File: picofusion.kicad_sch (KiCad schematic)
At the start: 48 parts, among them J1 NORTH, J2 EAST, J3 WEST, J4 SOUTH, U1 W25Q16, U2 RP2040, U3 TLV71333PDQN, U7 TJA1051TK-3, Y1 12MHz

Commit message: finish R02B
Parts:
- removed 3V3: TestPoint, TestPoint:TestPoint_Pad_1.0x1.0mm, symbol Connector:TestPoint
- added R24: 0, Resistor_SMD:R_0402_1005Metric, symbol Device:R
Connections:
- net SD_nCD: now also R24.2
- net SPI0_nCS: now also R24.1
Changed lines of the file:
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@@
 (kicad_sch (version 20211123) (generator eeschema)
   (paper "A4")
-  (junction (at 204.47 85.09) (diameter 0) (color 0 0 0 0)
-  )
   (junction (at 66.04 24.13) (diameter 0.9144) (color 0 0 0 0)
   )
@@
   (junction (at 99.06 36.83) (diameter 0.9144) (color 0 0 0 0)
   )
-  (no_connect (at 96.52 128.27))
   (no_connect (at 96.52 110.49))
+  (no_connect (at 96.52 128.27))
   (no_connect (at 96.52 130.81))
+  (no_connect (at 96.52 92.71))
   (no_connect (at 96.52 90.17))
   (no_connect (at 96.52 85.09))
-  (no_connect (at 96.52 92.71))
   (wire (pts (xy 96.52 77.47) (xy 114.3 77.47))
     (stroke (width 0) (type default) (color 0 0 0 0))
@@
     (stroke (width 0) (type default) (color 0 0 0 0))
   )
-  (wire (pts (xy 204.47 85.09) (xy 204.47 82.55))
-    (stroke (width 0) (type default) (color 0 0 0 0))
-  )
   (wire (pts (xy 121.92 34.29) (xy 121.92 36.83))
     (stroke (width 0) (type default) (color 0 0 0 0))
@@
     (stroke (width 0) (type solid) (color 0 0 0 0))
   )
+  (wire (pts (xy 219.71 74.93) (xy 237.49 74.93))
+    (stroke (width 0) (type default) (color 0 0 0 0))
+  )
   (wire (pts (xy 96.52 44.45) (xy 113.03 44.45))
     (stroke (width 0) (type solid) (color 0 0 0 0))
@@
     (stroke (width 0) (type default) (color 0 0 0 0))
   )
-  (wire (pts (xy 262.89 74.93) (xy 247.65 74.93))
+  (wire (pts (xy 245.11 74.93) (xy 262.89 74.93))
     (stroke (width 0) (type default) (color 0 0 0 0))
   )
@@
     (stroke (width 0) (type default) (color 0 0 0 0))
   )
-  (wire (pts (xy 199.39 85.09) (xy 204.47 85.09))
+  (wire (pts (xy 199.39 85.09) (xy 207.01 85.09))
     (stroke (width 0) (type default) (color 0 0 0 0))
   )
@@
     (stroke (width 0) (type default) (color 0 0 0 0))
   )
-  (wire (pts (xy 204.47 85.09) (xy 207.01 85.09))
-    (stroke (width 0) (type default) (color 0 0 0 0))
-  )
   (wire (pts (xy 19.05 24.13) (xy 25.4 24.13))
     (stroke (width 0) (type default) (color 0 0 0 0))
@@
     (effects (font (size 1.27 1.27)) (justify right bottom))
   )
+  (label "SPI0_nCS" (at 219.71 74.93 0)
+    (effects (font (size 1.27 1.27)) (justify left bottom))
+  )
   (label "SPI0_PICO" (at 162.56 33.02 0)
     (effects (font (size 1.27 1.27)) (justify left bottom))
@@
     (pin "1")
   )
+  (symbol (lib_id "Device:R") (at 241.3 74.93 90) (unit 1)
+    (in_bom yes) (on_board yes)
+    (property "Reference" "R24" (id 0) (at 241.3 69.85 90))
+    (property "Value" "0" (id 1) (at 241.3 74.93 90))
+    (property "Footprint" "Resistor_SMD:R_0402_1005Metric" (id 2) (at 241.3 76.708 90)
+      (effects (font (size 1.27 1.27)) hide)
+    )
+    (property "Datasheet" "~" (id 3) (at 241.3 74.93 0)
+      (effects (font (size 1.27 1.27)) hide)
+    )
+    (property "DNP" "[DNP]" (id 4) (at 241.3 72.39 90))
+    (pin "1")
+    (pin "2")
+  )
   (symbol (lib_id "Device:C") (at 199.39 91.44 0) (unit 1)
     (in_bom yes) (on_board yes) (fields_autoplaced)
@@
     (pin "1")
   )
-  (symbol (lib_id "Connector:TestPoint") (at 204.47 82.55 0) (unit 1)
-    (in_bom yes) (on_board yes)
-    (property "Reference" "3V3" (id 0) (at 203.2 77.47 0)
-      (effects (font (size 1.27 1.27)) (justify left))
-    )
-    (property "Value" "TestPoint" (id 1) (at 207.01 80.5179 0)
-      (effects (font (size 1.27 1.27)) (justify left) hide)
-    )
-    (property "Footprint" "TestPoint:TestPoint_Pad_1.0x1.0mm" (id 2) (at 209.55 82.55 0)
-      (effects (font (size 1.27 1.27)) hide)
-    )
-    (property "Datasheet" "~" (id 3) (at 209.55 82.55 0)
-      (effects (font (size 1.27 1.27)) hide)
-    )
-    (pin "1")
-  )
   (symbol (lib_id "Device:C") (at 91.44 30.48 0) (unit 1)
     (in_bom yes) (on_board yes)
@@
       (reference "#PWR0111") (unit 1) (value "GND") (footprint "")
     )
-    (path "/5f13a28e-82a1-4e85-b4bc-5dfc256ed5f9"
-      (reference "3V3") (unit 1) (value "TestPoint") (footprint "TestPoint:TestPoint_Pad_1.0x1.0mm")
-    )
     (path "/d7b2b70b-51e8-4c92-820a-d9481fe18140"
       (reference "C1") (unit 1) (value "0.1uF") (footprint "Capacitor_SMD:C_0402_1005Metric")
@@
       (reference "R23") (unit 1) (value "10K") (footprint "Resistor_SMD:R_0402_1005Metric")
     )
+    (path "/1bc91197-611a-43de-a0c8-4847d4e8d56c"
+      (reference "R24") (unit 1) (value "0") (footprint "Resistor_SMD:R_0402_1005Metric")
+    )
     (path "/2b6f5c8a-05cf-4448-8322-d77121105d11"

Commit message: R02B: finish new discussion modifications
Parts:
- removed J1: NORTH, picofusion_stamp:Castellated_1x8_P2.54mm_Vertical, symbol Connector_Generic:Conn_01x08
- removed R22, R24: 0, Resistor_SMD:R_0402_1005Metric, symbol Device:R
- added J1: NORTH, Connector_PinHeader_2.00mm:PinHeader_1x10_P2.00mm_Vertical, symbol Connector_Generic:Conn_01x10
- C1, C10, C11, C13, C15, C2, C24, C26, C27, C28, C4, C6, C7, C9: footprint Capacitor_SMD:C_0402_1005Metric -> Capacitor_SMD:C_0201_0603Metric; Mfr. # (none) -> CC0201KRX5R5BB104
- C14, C16: footprint Capacitor_SMD:C_0402_1005Metric -> Capacitor_SMD:C_0603_1608Metric
- C25, C3: footprint Capacitor_SMD:C_0402_1005Metric -> Capacitor_SMD:C_0201_0603Metric
- J2, J3, J4: footprint picofusion_stamp:Castellated_1x8_P2.54mm_Vertical -> Connector_PinHeader_2.00mm:PinHeader_1x10_P2.00mm_Vertical; symbol Connector_Generic:Conn_01x08 -> Connector_Generic:Conn_01x10
- R1, R2, R20, R3: footprint Resistor_SMD:R_0402_1005Metric -> Resistor_SMD:R_0201_0603Metric
- R21: DNP [DNP] -> (none)
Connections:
- net SCL/SCK is gone; now on net SPI0_SCK: J3.2 (Pin_2)
- net SDA/SDI is gone; now on net SPI0_nCS: J3.1 (Pin_1)
- net +3V3: now also J3.6 (Pin_6); no longer J3.5 (Pin_5)
- net +5V: now also J3.10 (Pin_10), J1.8 (Pin_8); no longer J4.1 (Pin_1)
- net BOOTSEL: now also J2.10 (Pin_10)
- net CAN_N: now also J3.7 (Pin_7); no longer J3.6 (Pin_6)
- net CAN_P: now also J3.8 (Pin_8); no longer J3.7 (Pin_7)
- net GND: now also J2.6 (Pin_6), J3.9 (Pin_9), J1.5 (Pin_5), J1.9 (Pin_9); no longer J2.8 (Pin_8), J3.8 (Pin_8)
- net RUN: now also J2.9 (Pin_9)
- net SPI0_PICO: now also J3.3 (Pin_3)
- net SPI0_POCI: now also J3.4 (Pin_4); no longer J3.3 (Pin_3)
- net SWCLK: now also J4.9 (Pin_9)
- net SWDIO: now also J4.10 (Pin_10)
- net UART1_RX_GNSS: now also J2.7 (Pin_7); no longer J2.6 (Pin_6)
- net UART1_TX_GNSS: now also J2.8 (Pin_8); no longer J2.7 (Pin_7)
- net USB_DN: now also J1.7 (Pin_7)
- net USB_DP: now also J1.6 (Pin_6)
- net DRDY_ICM20602 renamed DRDY_ICM42605
- net DRDY_ICM42605: now also J3.5 (Pin_5)
- net NEOPIXEL renamed LED
- net LED: now also J4.1 (Pin_1); no longer J3.4 (Pin_4)
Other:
- sheet Sensor Suite ports: added DRDY_ICM42605; removed DRDY_ICM20602, SCL/SCK, SDA/SDI

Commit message: more board cleanup, silkscreen draft
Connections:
- net +5V: now also J1.9 (Pin_9); no longer J1.8 (Pin_8)
- net GND: now also J1.10 (Pin_10), J1.8 (Pin_8); no longer J1.5 (Pin_5), J1.9 (Pin_9)
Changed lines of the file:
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@@
   (junction (at 60.96 24.13) (diameter 0.9144) (color 0 0 0 0)
   )
-  (junction (at 260.35 48.26) (diameter 0) (color 0 0 0 0)
-  )
   (junction (at 106.68 24.13) (diameter 0.9144) (color 0 0 0 0)
   )
@@
   )
   (junction (at 99.06 36.83) (diameter 0.9144) (color 0 0 0 0)
+  )
+  (junction (at 260.35 50.8) (diameter 0) (color 0 0 0 0)
   )
   (no_connect (at 96.52 110.49))
@@
     (stroke (width 0) (type default) (color 0 0 0 0))
   )
+  (wire (pts (xy 257.81 48.26) (xy 262.89 48.26))
+    (stroke (width 0) (type default) (color 0 0 0 0))
+  )
   (wire (pts (xy 96.52 125.73) (xy 114.3 125.73))
     (stroke (width 0) (type default) (color 0 0 0 0))
@@
     (stroke (width 0) (type default) (color 0 0 0 0))
   )
-  (wire (pts (xy 260.35 48.26) (xy 260.35 50.8))
+  (wire (pts (xy 260.35 50.8) (xy 260.35 53.34))
     (stroke (width 0) (type default) (color 0 0 0 0))
   )
@@
     (stroke (width 0) (type default) (color 0 0 0 0))
   )
+  (wire (pts (xy 262.89 45.72) (xy 260.35 45.72))
+    (stroke (width 0) (type default) (color 0 0 0 0))
+  )
   (wire (pts (xy 120.65 46.99) (xy 130.81 46.99))
     (stroke (width 0) (type solid) (color 0 0 0 0))
@@
     (stroke (width 0) (type solid) (color 0 0 0 0))
   )
+  (wire (pts (xy 260.35 45.72) (xy 260.35 50.8))
+    (stroke (width 0) (type default) (color 0 0 0 0))
+  )
   (wire (pts (xy 19.05 34.29) (xy 19.05 36.83))
     (stroke (width 0) (type default) (color 0 0 0 0))
@@
     (stroke (width 0) (type solid) (color 0 0 0 0))
   )
-  (wire (pts (xy 260.35 38.1) (xy 260.35 48.26))
-    (stroke (width 0) (type default) (color 0 0 0 0))
-  )
   (wire (pts (xy 154.94 143.51) (xy 154.94 144.78))
     (stroke (width 0) (type default) (color 0 0 0 0))
@@
     (stroke (width 0) (type solid) (color 0 0 0 0))
   )
-  (wire (pts (xy 262.89 38.1) (xy 260.35 38.1))
-    (stroke (width 0) (type default) (color 0 0 0 0))
-  )
   (wire (pts (xy 80.01 162.56) (xy 80.01 160.02))
     (stroke (width 0) (type default) (color 0 0 0 0))
@@
     (stroke (width 0) (type solid) (color 0 0 0 0))
   )
-  (wire (pts (xy 260.35 48.26) (xy 262.89 48.26))
+  (wire (pts (xy 260.35 50.8) (xy 262.89 50.8))
     (stroke (width 0) (type default) (color 0 0 0 0))
   )
@@
   )
   (wire (pts (xy 96.52 74.93) (xy 114.3 74.93))
-    (stroke (width 0) (type default) (color 0 0 0 0))
-  )
-  (wire (pts (xy 257.81 45.72) (xy 262.89 45.72))
     (stroke (width 0) (type default) (color 0 0 0 0))
   )
@@
     (pin "2")
   )
-  (symbol (lib_id "power:+5V") (at 257.81 45.72 90) (unit 1)
-    (in_bom yes) (on_board yes) (fields_autoplaced)
-    (property "Reference" "#PWR0110" (id 0) (at 261.62 45.72 0)
-      (effects (font (size 1.27 1.27)) hide)
-    )
-    (property "Value" "+5V" (id 1) (at 254 45.7199 90)
-      (effects (font (size 1.27 1.27)) (justify left))
-    )
-    (property "Footprint" "" (id 2) (at 257.81 45.72 0)
-      (effects (font (size 1.27 1.27)) hide)
-    )
-    (property "Datasheet" "" (id 3) (at 257.81 45.72 0)
+  (symbol (lib_id "power:+5V") (at 257.81 48.26 90) (unit 1)
+    (in_bom yes) (on_board yes) (fields_autoplaced)
+    (property "Reference" "#PWR0110" (id 0) (at 261.62 48.26 0)
+      (effects (font (size 1.27 1.27)) hide)
+    )
+    (property "Value" "+5V" (id 1) (at 254 48.2599 90)
+      (effects (font (size 1.27 1.27)) (justify left))
+    )
+    (property "Footprint" "" (id 2) (at 257.81 48.26 0)
+      (effects (font (size 1.27 1.27)) hide)
+    )
+    (property "Datasheet" "" (id 3) (at 257.81 48.26 0)
       (effects (font (size 1.27 1.27)) hide)
     )
@@
     (pin "1")
   )
-  (symbol (lib_id "power:GND") (at 260.35 50.8 0) (unit 1)
-    (in_bom yes) (on_board yes) (fields_autoplaced)
-    (property "Reference" "#PWR0105" (id 0) (at 260.35 57.15 0)
-      (effects (font (size 1.27 1.27)) hide)
-    )
-    (property "Value" "GND" (id 1) (at 260.35 55.88 0))
-    (property "Footprint" "" (id 2) (at 260.35 50.8 0)
-      (effects (font (size 1.27 1.27)) hide)
-    )
-    (property "Datasheet" "" (id 3) (at 260.35 50.8 0)
-      (effects (font (size 1.27 1.27)) hide)
-    )
+  (symbol (lib_id "power:GND") (at 260.35 53.34 0) (unit 1)
+    (in_bom yes) (on_board yes) (fields_autoplaced)
+    (property "Reference" "#PWR0105" (id 0) (at 260.35 59.69 0)
+      (effects (font (size 1.27 1.27)) hide)
+    )
+    (property "Value" "GND" (id 1) (at 260.35 58.42 0))
+    (property "Footprint" "" (id 2) (at 260.35 53.34 0)
+      (effects (font (size 1.27 1.27)) hide)
+    )
+    (property "Datasheet" "" (id 3) (at 260.35 53.34 0)
+      (effects (font (size 1.27 1.27)) hide)
+    )

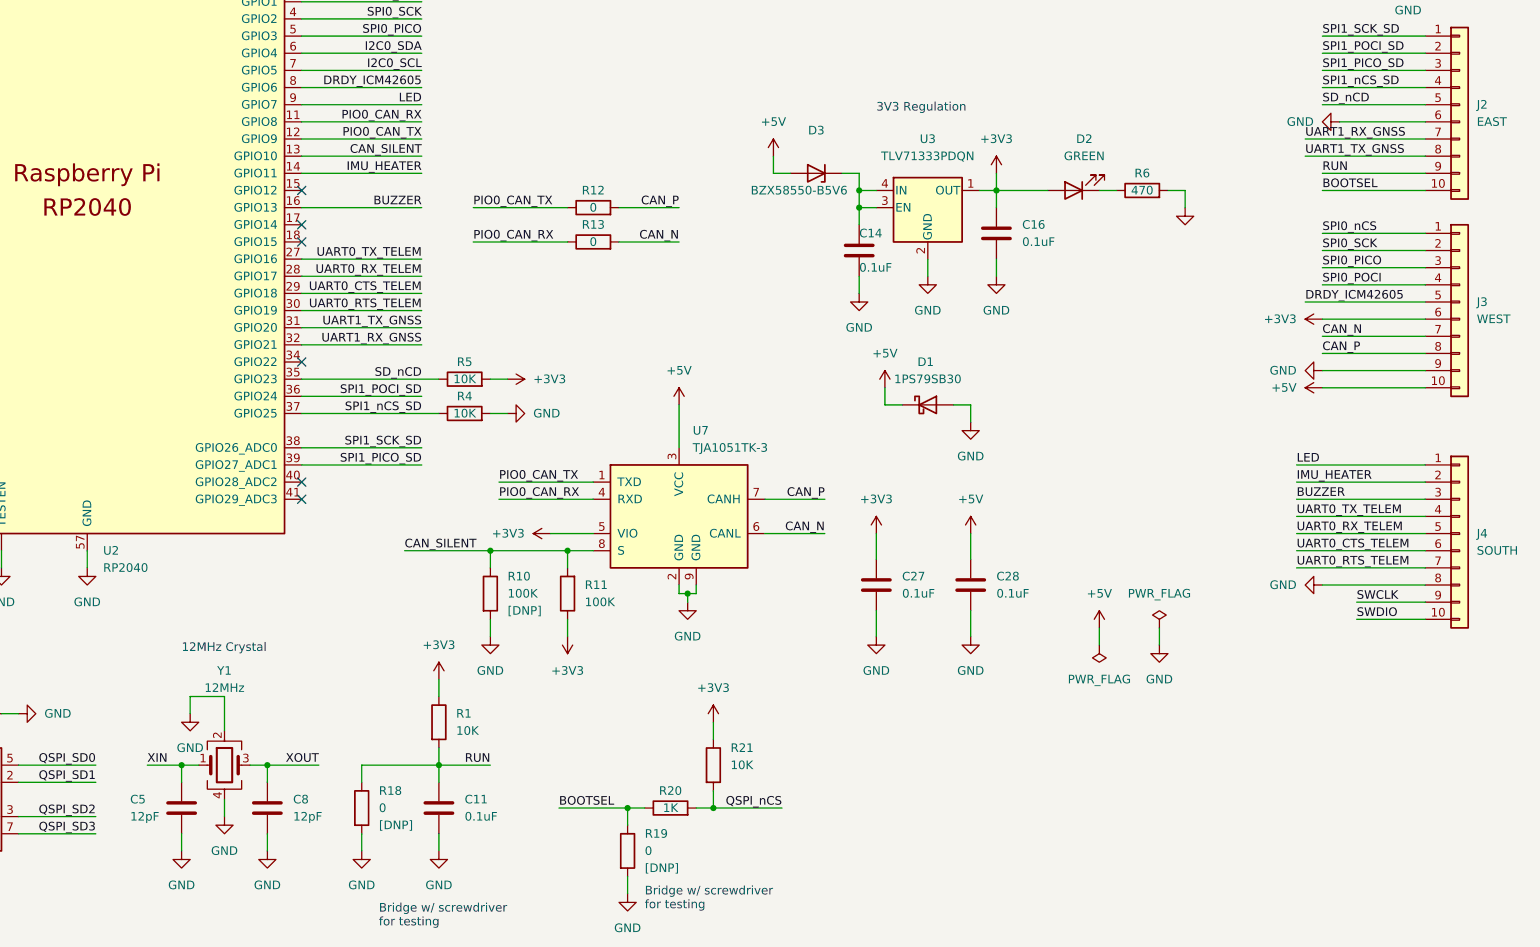
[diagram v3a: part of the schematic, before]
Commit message: update footprints, fix drc
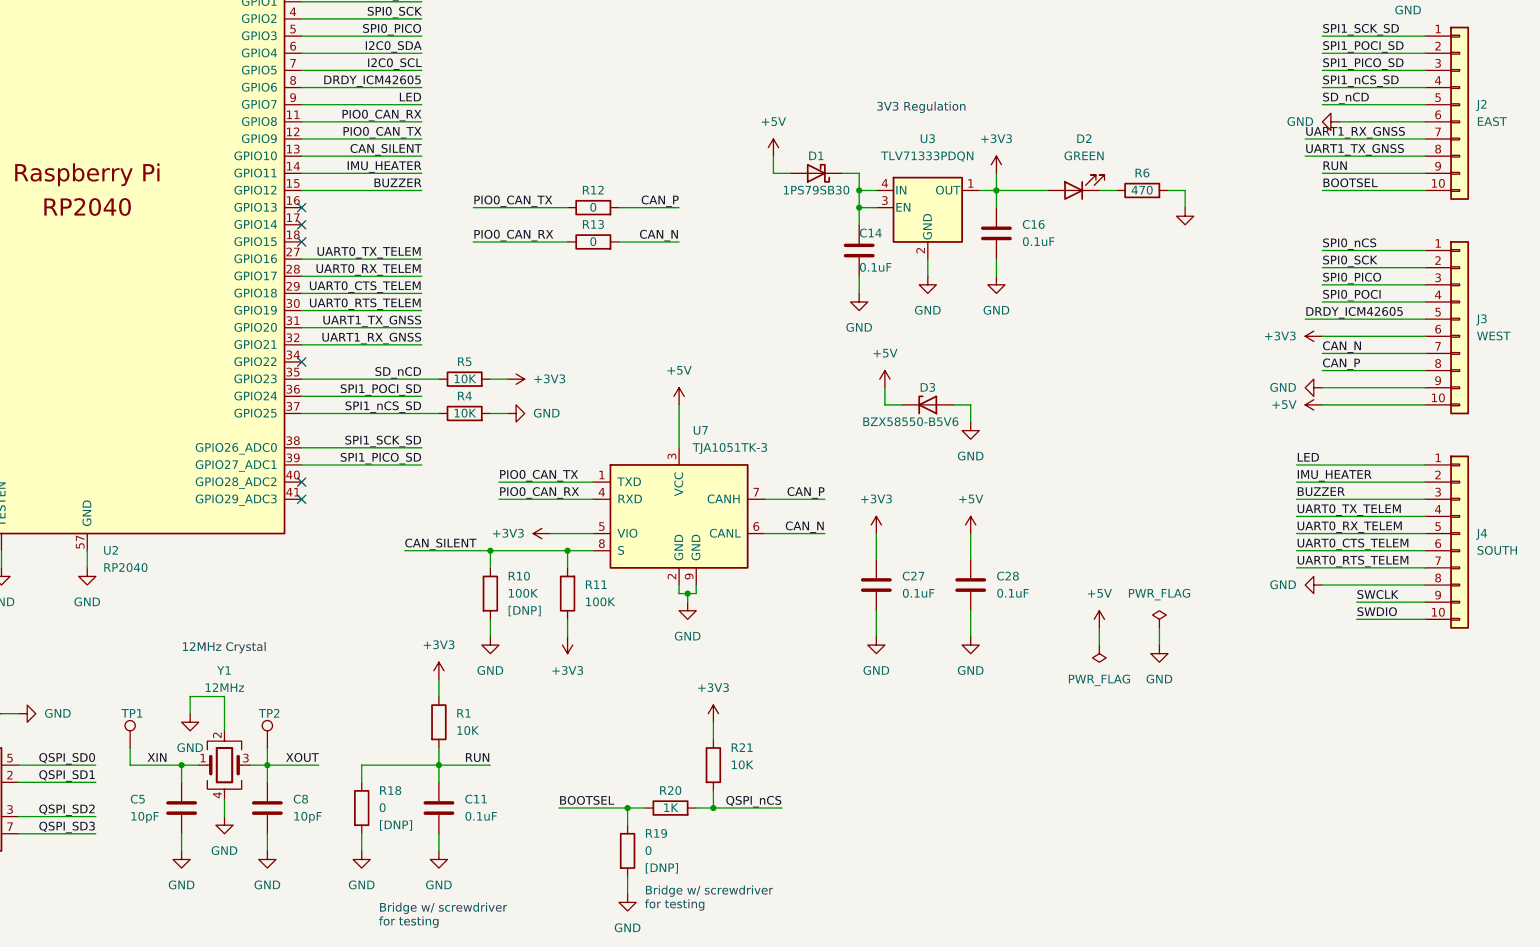
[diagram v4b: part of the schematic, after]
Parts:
- added TP1, TP2: TestPoint, TestPoint:TestPoint_Pad_D1.0mm, symbol Connector:TestPoint
- C5, C8: value 12pF -> 10pF
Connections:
- net +5V: now also D1.2 (A), D3.1 (K); no longer D1.1 (K), D3.2 (A)
- net BUZZER: now also U2.15 (GPIO12); no longer U2.16 (GPIO13)
- net GND: now also D3.2 (A); no longer D1.2 (A)
- net XIN: now also TP1.1
- net XOUT: now also TP2.1
- net at C14.1, U3.3 (EN), U3.4 (IN): now also D1.1 (K); no longer D3.1 (K)
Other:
- moved on the sheet: D1, D3, J3
